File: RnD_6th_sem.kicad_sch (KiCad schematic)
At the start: 61 parts, among them IC1 2EDF7275KXUMA1, J1 HVDC1, J2 PWM, J3 HVDC2, J4 3.3V, J5 5V, J6 5V, J7 GND2, J8 GND1, Q1 IGLD60R190D1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

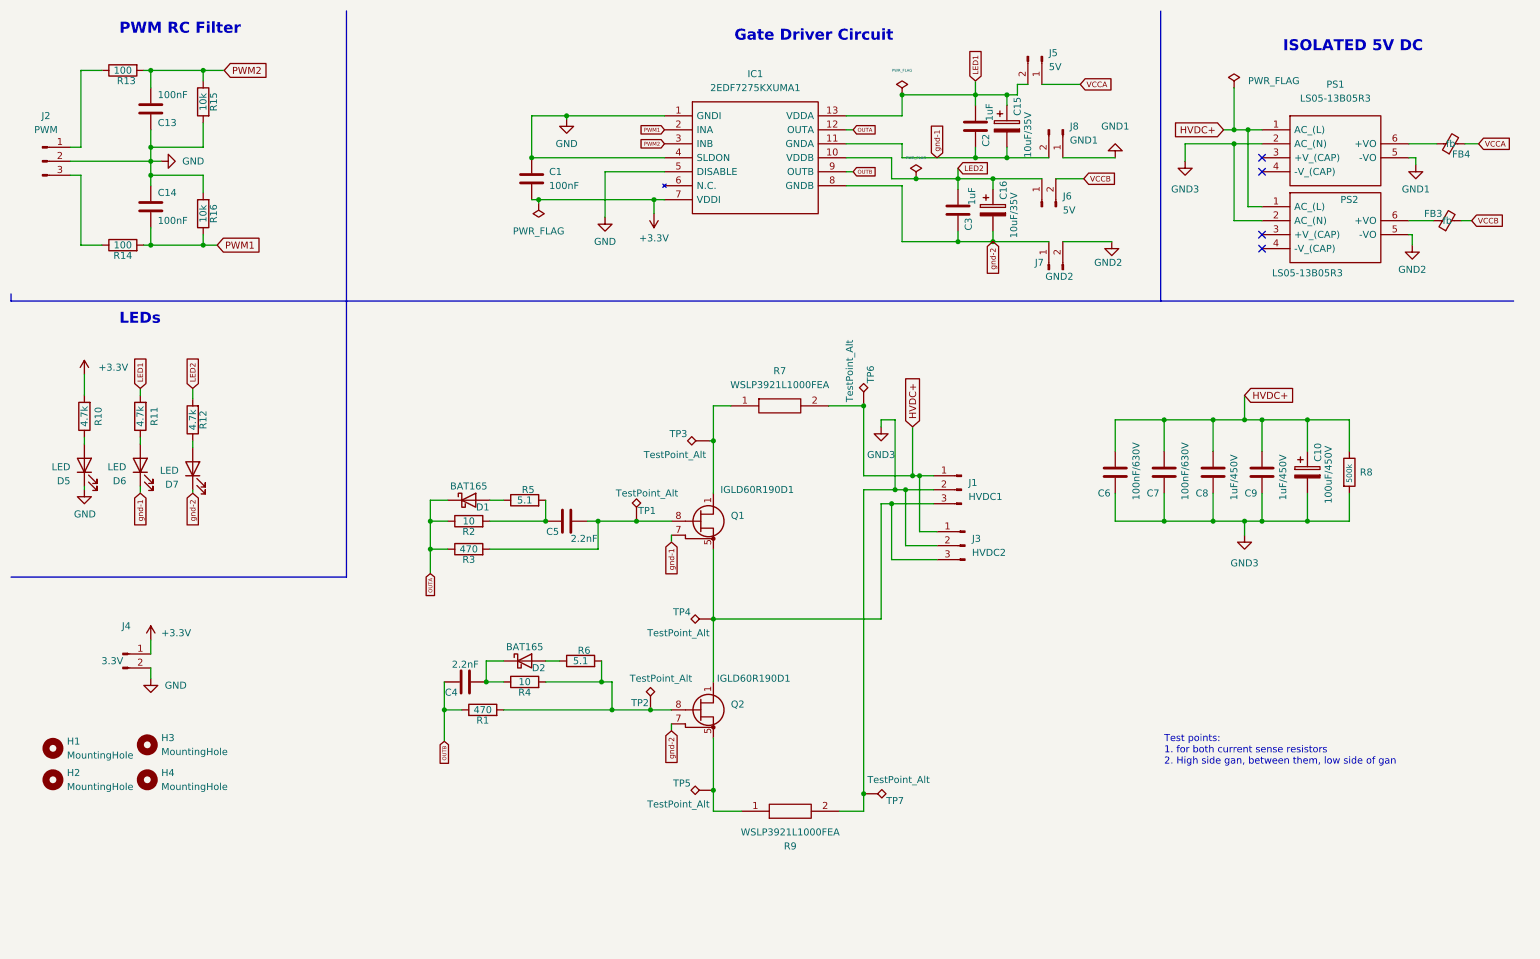
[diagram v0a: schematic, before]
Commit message: changed layout
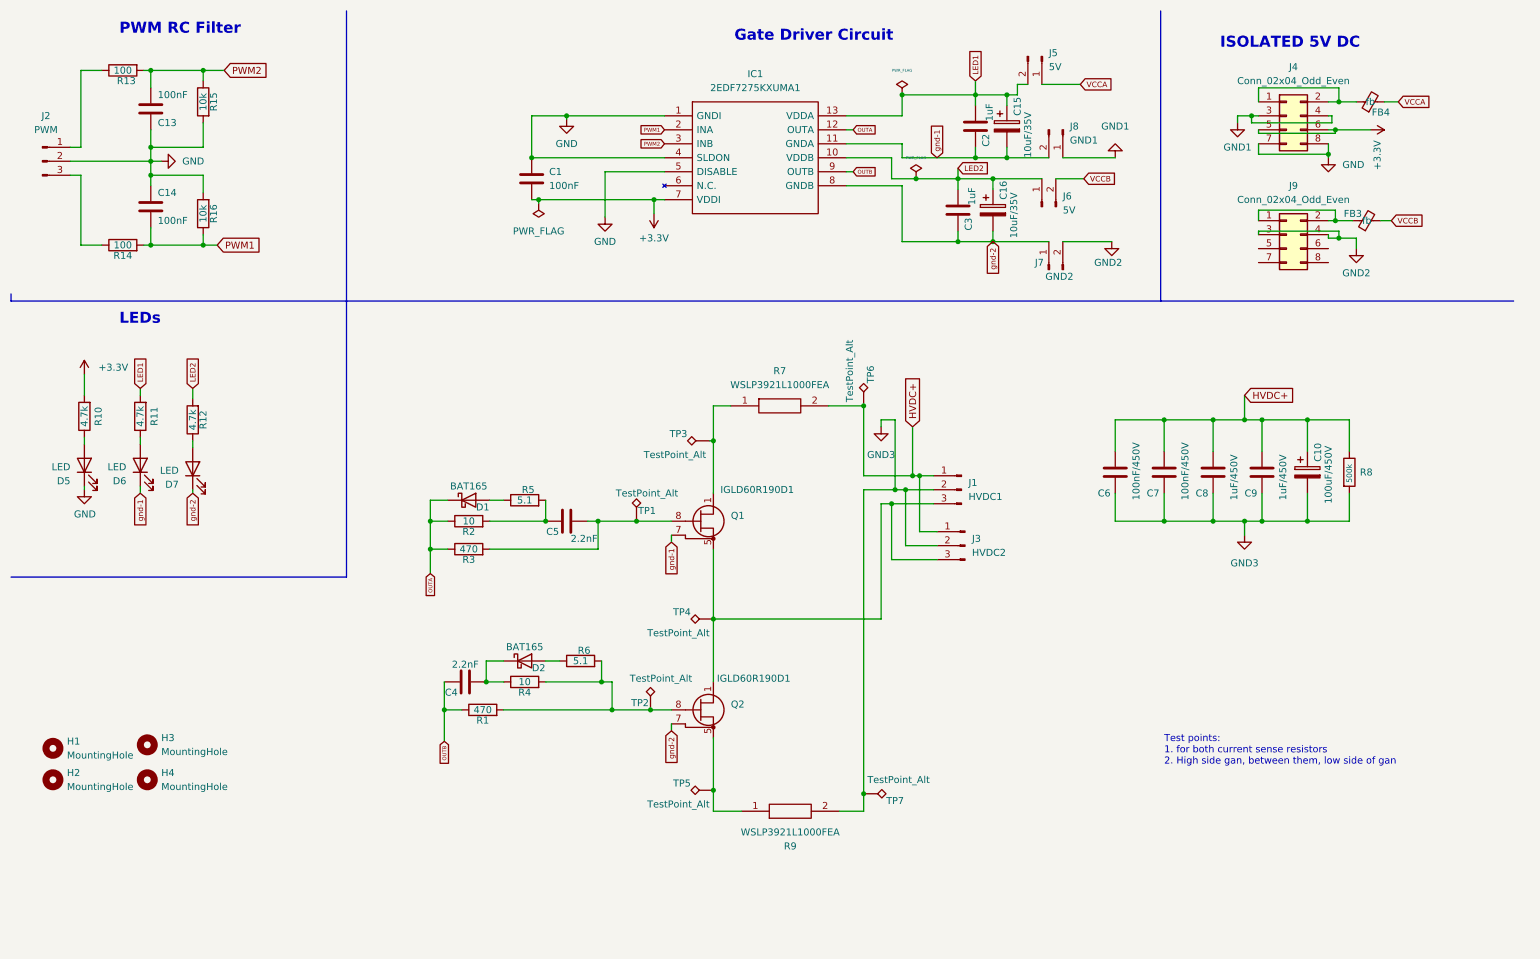
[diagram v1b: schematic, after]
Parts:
- removed J4: 3.3V, Connector_Molex:Molex_KK-254_AE-6410-02A_1x02_P2.54mm_Vertical, symbol Connector:Conn_01x02_Male
- removed PS1, PS2: LS05-13B05R3, footprint&lib:LS0513B05R3, symbol LS05-13B05R3:LS05-13B05R3
- added J4, J9: Conn_02x04_Odd_Even, Connector_IDC:IDC-Header_2x04_P2.54mm_Vertical, symbol Connector_Generic:Conn_02x04_Odd_Even
- C6, C7: value 100nF/630V -> 100nF/450V
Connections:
- net +3.3V: now also J4.5 (Pin_5), J4.6 (Pin_6)
- net GND: now also J4.7 (Pin_7), J4.8 (Pin_8)
- net GND1: now also J4.3 (Pin_3), J4.4 (Pin_4)
- net GND2: now also J9.3 (Pin_3), J9.4 (Pin_4)
- net at FB3.1: now also J9.1 (Pin_1), J9.2 (Pin_2)
- net at FB4.1: now also J4.1 (Pin_1), J4.2 (Pin_2)
- no-connect marks 4 -> 0
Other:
- moved on the sheet: FB3, FB4

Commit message: changes done in schematic
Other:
- note added: "ISOLATED 5V DC and 3.3V DC"
- note removed: "ISOLATED 5V DC"
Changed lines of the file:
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@@
     (effects (font (size 2 2) (thickness 0.4) bold) (justify left bottom))
   )
-  (text "ISOLATED 5V DC" (at 231.775 19.05 0)
+  (text "ISOLATED 5V DC and 3.3V DC" (at 231.775 19.05 0)
     (effects (font (size 2 2) (thickness 0.4) bold) (justify left bottom))
   )

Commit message: added power board files
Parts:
- added FB1, FB2: fb, Resistor_SMD:R_0805_2012Metric, symbol Device:FerriteBead_Small
- added N1: Housing, Symbol:KiCad-Logo_20mm_SilkScreen, symbol Mechanical:Housing
- J4, J9: footprint Connector_IDC:IDC-Header_2x04_P2.54mm_Vertical -> Connector_PinSocket_2.54mm:PinSocket_2x04_P2.54mm_Vertical
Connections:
- net +3.3V: now also J9.7 (Pin_7), J9.8 (Pin_8); no longer J4.5 (Pin_5), J4.6 (Pin_6)
- net GND: now also J9.5 (Pin_5), J9.6 (Pin_6); no longer J4.7 (Pin_7), J4.8 (Pin_8)
- net GND1: now also FB1.1; no longer J4.3 (Pin_3), J4.4 (Pin_4)
- net GND2: now also FB2.2; no longer J9.3 (Pin_3), J9.4 (Pin_4)
- new net: FB2.1, J9.3 (Pin_3), J9.4 (Pin_4)
- new net: FB1.2, J4.5 (Pin_5), J4.6 (Pin_6)
- new net: FB4.1, J4.7 (Pin_7), J4.8 (Pin_8)
- now unconnected: J4.1 (Pin_1), J4.2 (Pin_2)
- no-connect marks 0 -> 4
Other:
- moved on the sheet: FB4, J4

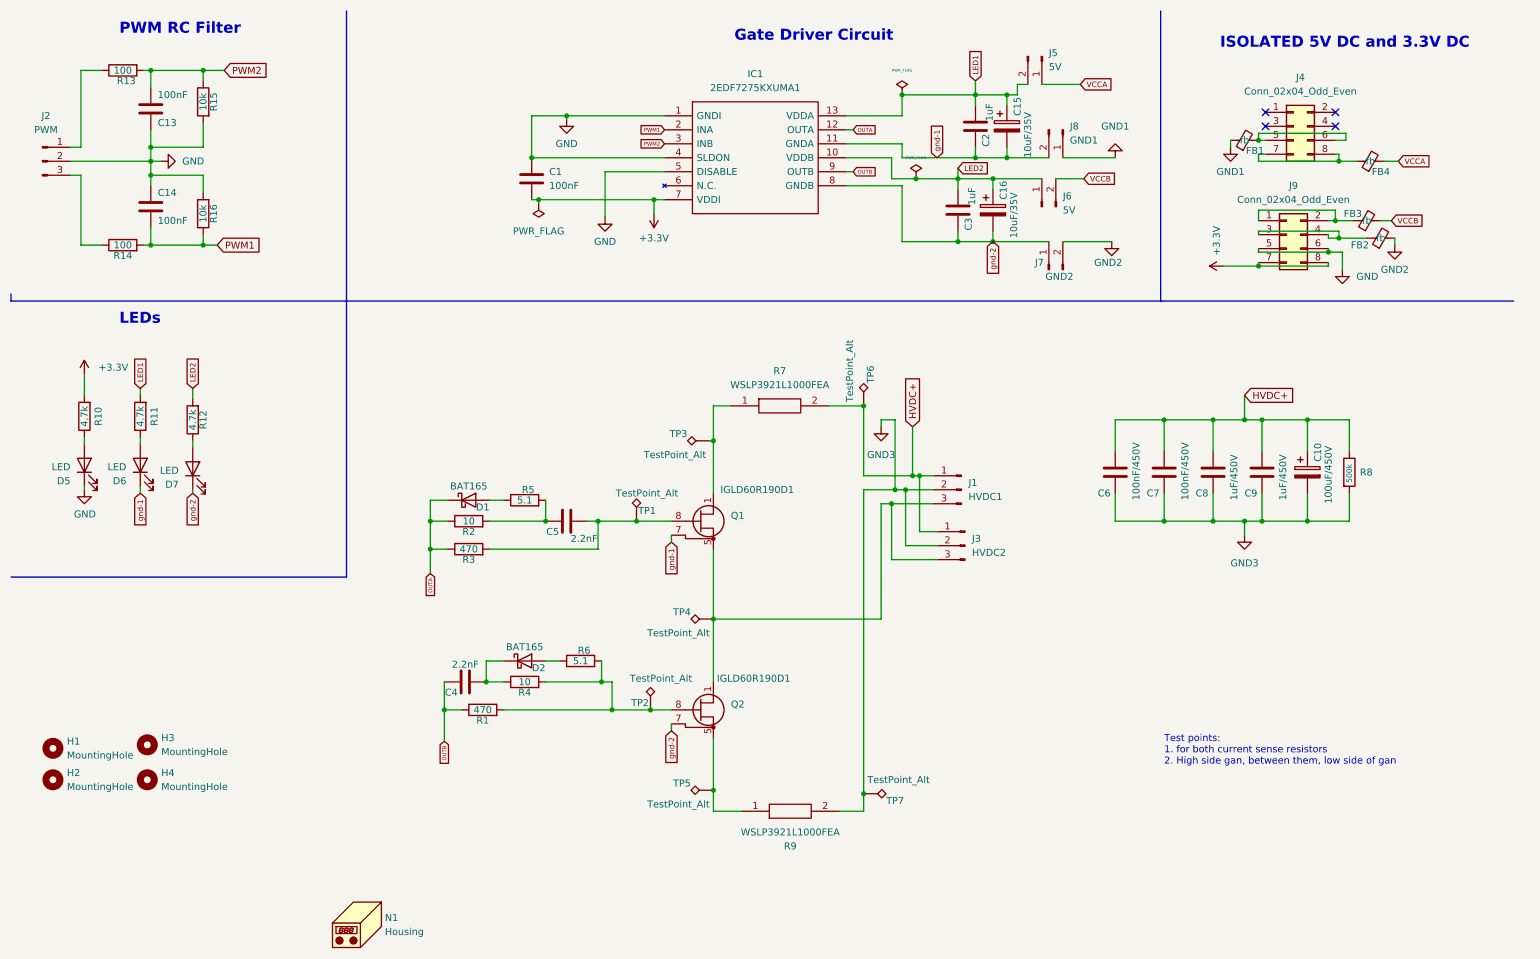
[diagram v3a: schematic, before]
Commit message: redesigned the power loop
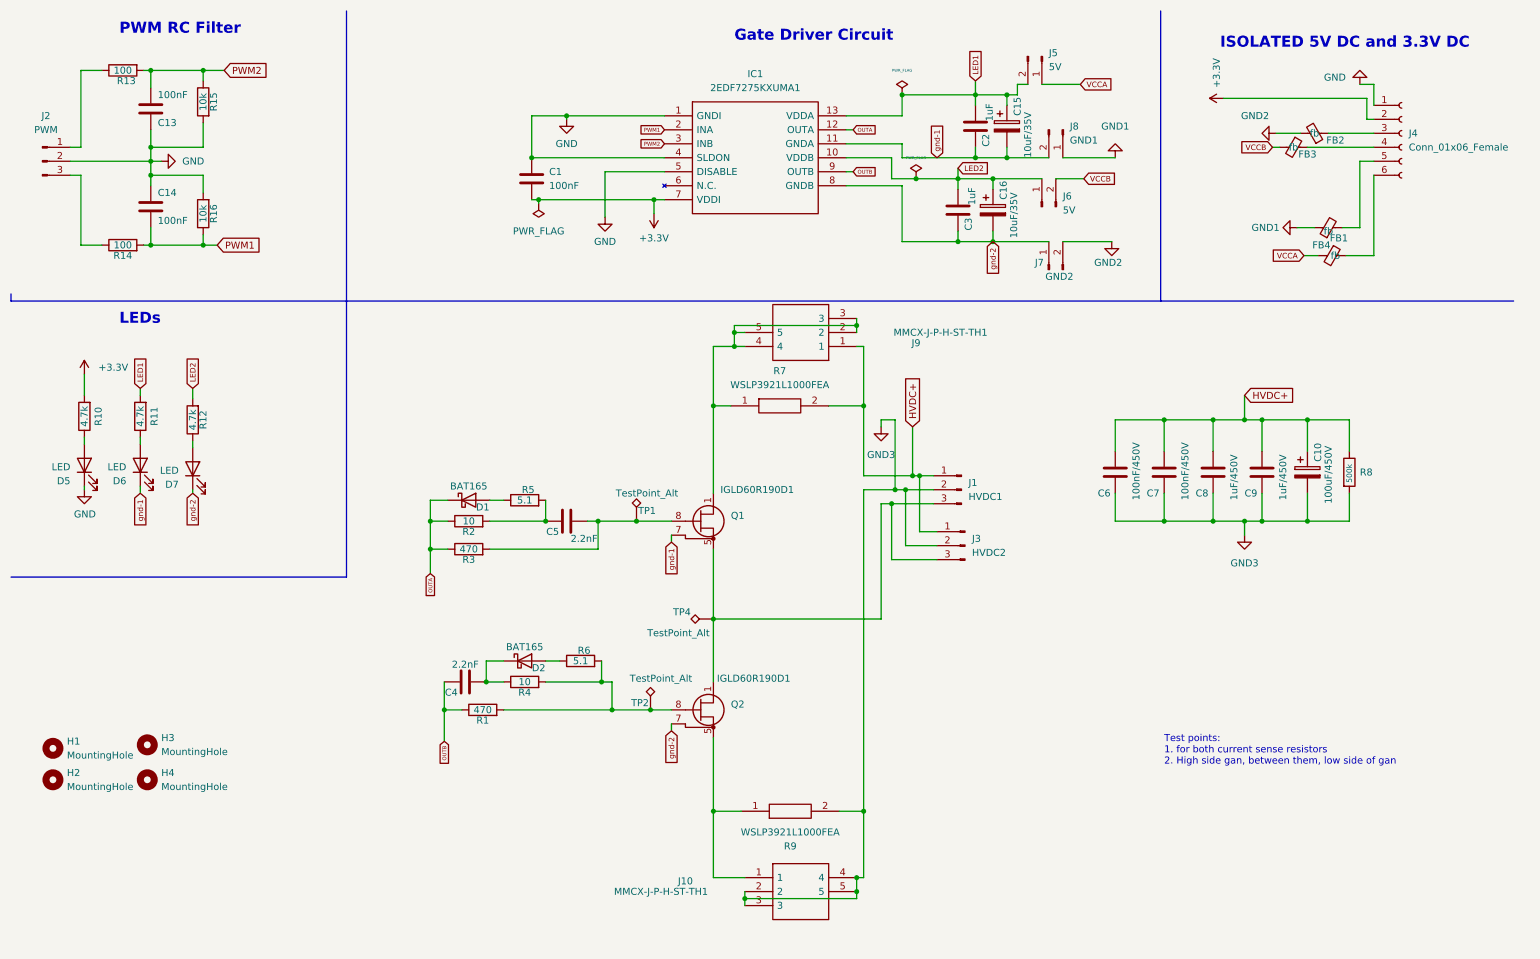
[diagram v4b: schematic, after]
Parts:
- removed J4, J9: Conn_02x04_Odd_Even, Connector_PinSocket_2.54mm:PinSocket_2x04_P2.54mm_Vertical, symbol Connector_Generic:Conn_02x04_Odd_Even
- removed N1: Housing, Symbol:KiCad-Logo_20mm_SilkScreen, symbol Mechanical:Housing
- removed TP3, TP5, TP6, TP7: TestPoint_Alt, TestPoint:TestPoint_THTPad_1.5x1.5mm_Drill0.7mm, symbol Connector:TestPoint_Alt
- added J10, J9: MMCX-J-P-H-ST-TH1, MMCX-J-P-H-ST-TH1:MMCXJPHSTTH1, symbol MMCX-J-P-H-ST-TH1:MMCX-J-P-H-ST-TH1
- added J4: Conn_01x06_Female, Connector_PinSocket_2.54mm:PinSocket_1x06_P2.54mm_Horizontal, symbol Connector:Conn_01x06_Female
- C1, C13, C14, C4, C5: footprint Capacitor_SMD:C_0805_2012Metric -> Capacitor_SMD:C_0402_1005Metric
- R1, R10, R11, R12, R13, R14, R15, R16, R2, R3, R4, R5, R6, R8: footprint Resistor_SMD:R_0805_2012Metric -> Resistor_SMD:R_0402_1005Metric
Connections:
- net +3.3V: now also J4.2 (Pin_2)
- net GND: now also J4.1 (Pin_1)
- net GND3: now also J10.2, J10.3, J10.4, J10.5
- net HVDC+: now also J9.1
- net at FB2.1: now also J4.3 (Pin_3)
- net at Q2.5 (S), Q2.6 (S), Q2.9 (S)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: now also J10.1
- net at FB3.1: now also J4.4 (Pin_4)
- net at Q1.1 (D), Q1.2 (D), Q1.3 (D)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: now also J9.2, J9.3, J9.4, J9.5
- net at FB1.2: now also J4.5 (Pin_5)
- net at FB4.1: now also J4.6 (Pin_6)
- no-connect marks 4 -> 0
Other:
- moved on the sheet: FB1, FB2, FB3, FB4

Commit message: updated schematic
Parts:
- C1, C13, C14, C4, C5: footprint Capacitor_SMD:C_0402_1005Metric -> Capacitor_SMD:C_0805_2012Metric
- C15, C16: footprint Capacitor_SMD:CP_Elec_4x5.8 -> Capacitor_SMD:CP_Elec_5x5.3
- C8, C9: value 1uF/450V -> 100nF/450V; footprint CGA9P4X7T2W105K250KA:CAPC5750X280N -> Capacitor_SMD:C_1206_3216Metric
- J1: value HVDC1 -> HVDC
- J3: value HVDC2 -> HVDC
- J7: value GND2 -> GND
- J8: value GND1 -> GND
- R1, R10, R11, R12, R13, R14, R15, R16, R2, R3, R4, R5, R6, R8: footprint Resistor_SMD:R_0402_1005Metric -> Resistor_SMD:R_0805_2012Metric

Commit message: Updated final design
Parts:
- removed J4: Conn_01x06_Female, Connector_PinSocket_2.54mm:PinSocket_1x06_P2.54mm_Horizontal, symbol Connector:Conn_01x06_Female
- added J4: Conn_02x05_Odd_Even, 61201021621:SHDR10W64P254_2X5_2036X885X925P, symbol Connector_Generic:Conn_02x05_Odd_Even
- IC1: footprint 2EDF7275KXUMA1:2EDF7275KXUMA1 -> 2EDF7275K:TFLGA65P500X500X106-14_13N-V
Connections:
- net +3.3V: now also J4.2 (Pin_2)
- net GND: now also J4.1 (Pin_1)
- net at FB2.1: now also J4.3 (Pin_3)
- net at FB3.1: now also J4.4 (Pin_4)
- net at FB1.2: now also J4.5 (Pin_5)
- net at FB4.1: now also J4.6 (Pin_6)
- no-connect marks 0 -> 4
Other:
- moved on the sheet: FB1, FB2, FB3, FB4

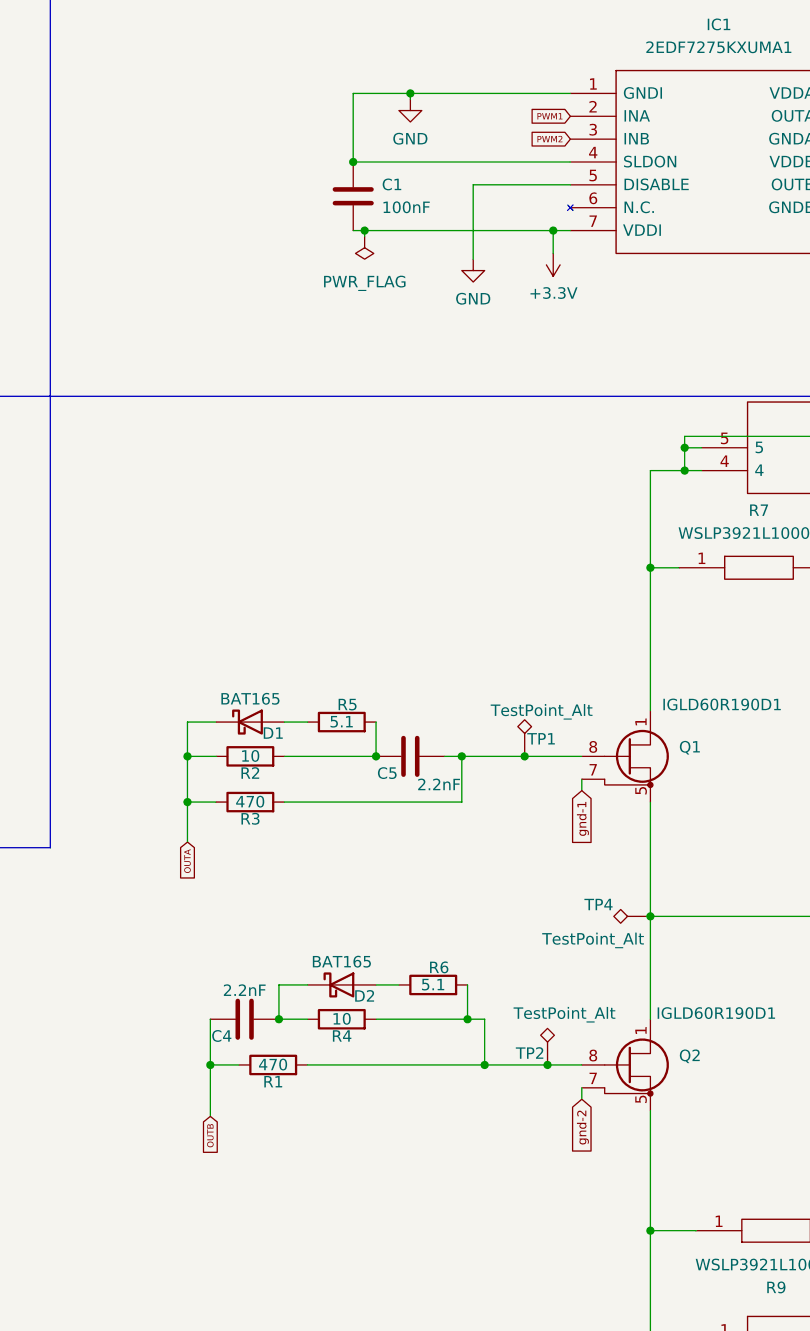
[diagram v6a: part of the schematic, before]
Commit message: updated design
optimized the size and layout
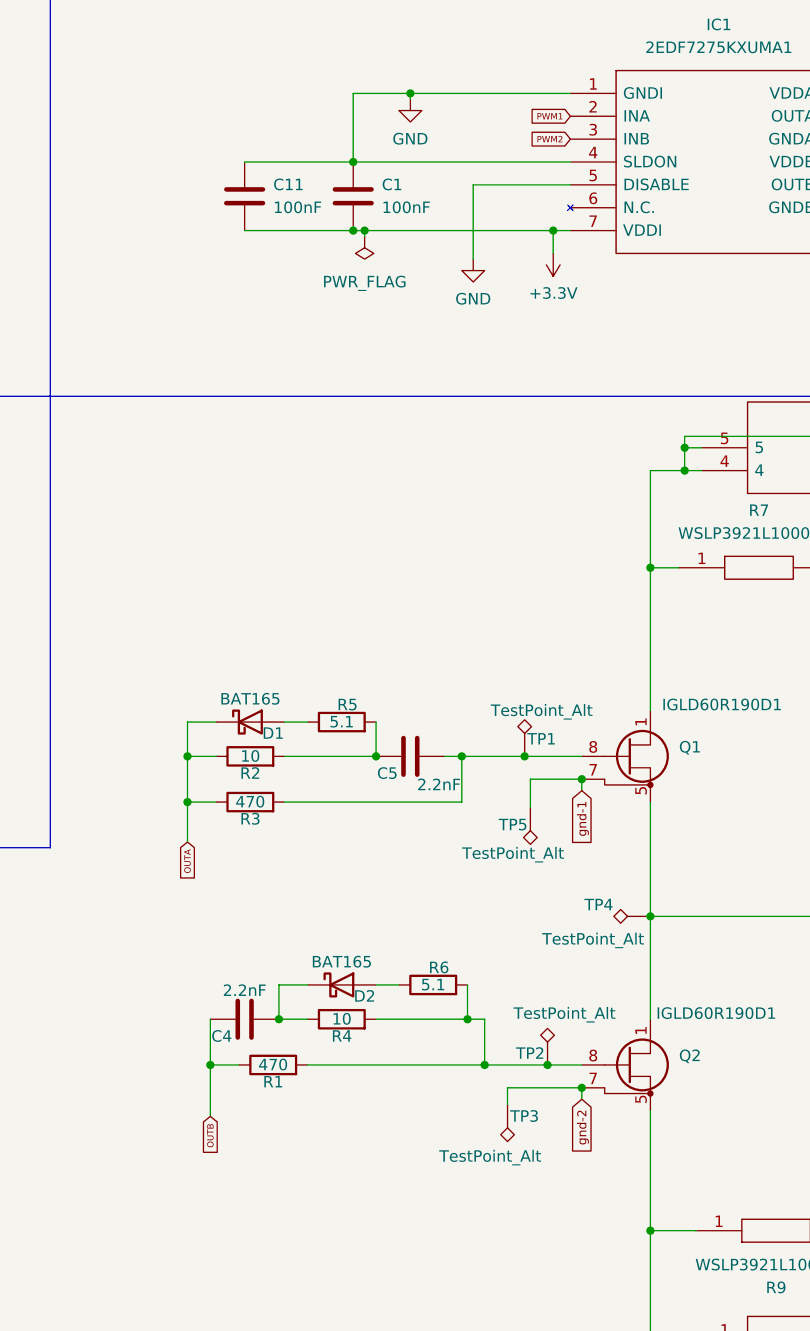
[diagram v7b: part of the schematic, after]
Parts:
- added C11: 100nF, Capacitor_SMD:C_0805_2012Metric, symbol Device:C
- added TP3, TP5: TestPoint_Alt, TestPoint:TestPoint_Keystone_5000-5004_Miniature, symbol Connector:TestPoint_Alt
- C10: footprint Capacitor_THT:CP_Radial_D18.0mm_P7.50mm -> EKXL451ELL101MM30S:CAPPRD750W80D1825H3200
- TP1, TP2, TP4: footprint TestPoint:TestPoint_THTPad_1.5x1.5mm_Drill0.7mm -> TestPoint:TestPoint_Keystone_5000-5004_Miniature
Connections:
- net +3.3V: now also C11.2
- net GND: now also C11.1
- net gnd-1: now also TP5.1
- net gnd-2: now also TP3.1
